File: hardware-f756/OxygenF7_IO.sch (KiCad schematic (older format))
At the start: 13 parts, among them J10 Micro_SD_Card_Det, J3 JST SH-4, J4 JST ZH-4, J5 Conn_03x08, J6 Conn_01x16, J7 Conn_01x04, J9 JST GH-6, U3 MPU-6000, U4 BMP388

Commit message: Swap out some out-of-stock parts
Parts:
- C19, C20, C22: Part# CL21B104KACNNNC -> CL21B104KBCNNNC‎
- C21: Part# CL21B104KACNNNC -> CL21B222KBANNNC
- J3: footprint Connector_JST:JST_SH_BM04B-SRSS-TB_1x04-1MP_P1.00mm_Vertical -> Connector_JST:JST_SH_SM04B-SRSS-TB_1x04-1MP_P1.00mm_Horizontal; Part# BM04B-SRSS-TB(LF)(SN) -> SM04B-SRSS-TB(LF)(SN)
- J9: value JST GH-6 -> 1.25mm; footprint Connector_JST:JST_GH_BM06B-GHS-TBT_1x06-1MP_P1.25mm_Vertical -> Sonrise:10114830-10106LF_P1.25mm_Horizontal; Part# BM04B-GHS-TBT(LF)(SN)(N) -> 10114830-10106LF
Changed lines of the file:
@@
 F 0 "J3" H 4068 775 50  0000 C CNN
 F 1 "JST SH-4" H 4068 866 50  0000 C CNN
-F 2 "Connector_JST:JST_SH_BM04B-SRSS-TB_1x04-1MP_P1.00mm_Vertical" H 4150 1200 50  0001 C CNN
+F 2 "Connector_JST:JST_SH_SM04B-SRSS-TB_1x04-1MP_P1.00mm_Horizontal" H 4150 1200 50  0001 C CNN
 F 3 "~" H 4150 1200 50  0001 C CNN
-F 4 "BM04B-SRSS-TB(LF)(SN)" H 4150 1200 50  0001 C CNN "Part#"
+F 4 "SM04B-SRSS-TB(LF)(SN)" H 4150 1200 50  0001 C CNN "Part#"
 	1    4150 1200
 	-1   0    0    1
@@
 F 2 "Capacitor_SMD:C_0805_2012Metric" H 2488 3450 50  0001 C CNN
 F 3 "~" H 2450 3600 50  0001 C CNN
-F 4 "CL21B104KACNNNC" H 2450 3600 50  0001 C CNN "Part#"
+F 4 "CL21B104KBCNNNC‎" H 2450 3600 50  0001 C CNN "Part#"
 	1    2450 3600
 	1    0    0    -1
@@
 F 2 "Capacitor_SMD:C_0805_2012Metric" H 3088 2000 50  0001 C CNN
 F 3 "~" H 3050 2150 50  0001 C CNN
-F 4 "CL21B104KACNNNC" H 3050 2150 50  0001 C CNN "Part#"
+F 4 "CL21B222KBANNNC" H 3050 2150 50  0001 C CNN "Part#"
 	1    3050 2150
 	1    0    0    -1
@@
 F 2 "Capacitor_SMD:C_0805_2012Metric" H 2688 2000 50  0001 C CNN
 F 3 "~" H 2650 2150 50  0001 C CNN
-F 4 "CL21B104KACNNNC" H 2650 2150 50  0001 C CNN "Part#"
+F 4 "CL21B104KBCNNNC‎" H 2650 2150 50  0001 C CNN "Part#"
 	1    2650 2150
 	1    0    0    -1
@@
 F 2 "Capacitor_SMD:C_0805_2012Metric" H 3538 1500 50  0001 C CNN
 F 3 "~" H 3500 1650 50  0001 C CNN
-F 4 "CL21B104KACNNNC" H 3500 1650 50  0001 C CNN "Part#"
+F 4 "CL21B104KBCNNNC‎" H 3500 1650 50  0001 C CNN "Part#"
 	1    3500 1650
 	1    0    0    -1
@@
 AR Path="/60FE74E7/61026A51" Ref="J9"  Part="1"
 F 0 "J9" H 4068 3075 50  0000 C CNN
-F 1 "JST GH-6" H 4068 3166 50  0000 C CNN
-F 2 "Connector_JST:JST_GH_BM06B-GHS-TBT_1x06-1MP_P1.25mm_Vertical" H 4150 3600 50  0001 C CNN
+F 1 "1.25mm" H 4068 3166 50  0000 C CNN
+F 2 "Sonrise:10114830-10106LF_P1.25mm_Horizontal" H 4150 3600 50  0001 C CNN
 F 3 "~" H 4150 3600 50  0001 C CNN
-F 4 "BM04B-GHS-TBT(LF)(SN)(N)" H 4150 3600 50  0001 C CNN "Part#"
+F 4 "10114830-10106LF" H 4150 3600 50  0001 C CNN "Part#"
 	1    4150 3600
 	-1   0    0    1

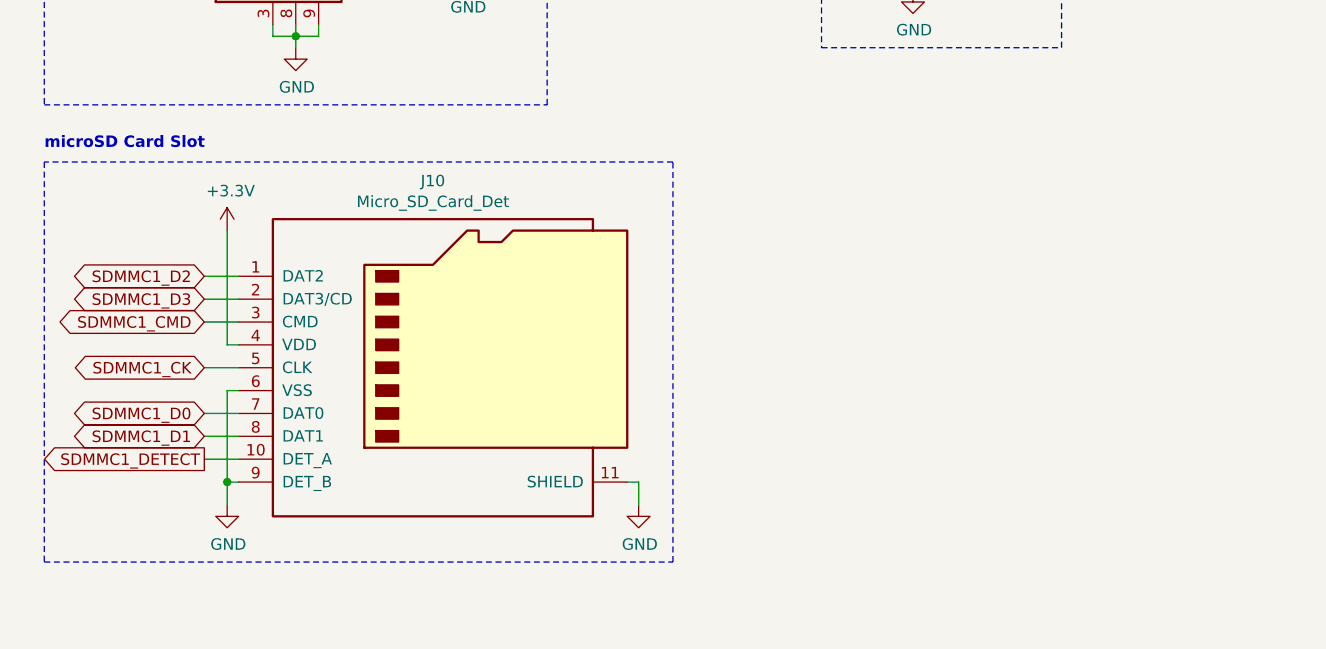
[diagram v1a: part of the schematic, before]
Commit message: Don't ground unused MCU pins and add microSD pull-up resistors
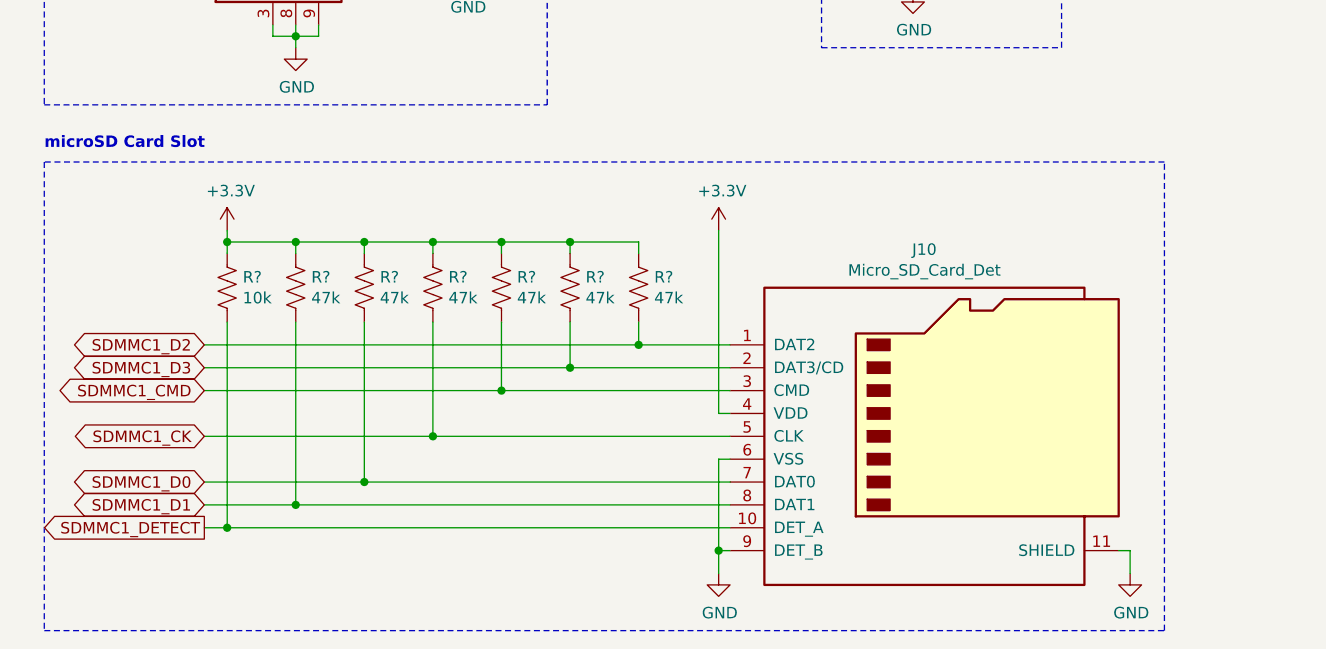
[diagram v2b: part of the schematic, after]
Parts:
- added R?: 10k, symbol Device:R_US
- added R? (x6): 47k, symbol Device:R_US
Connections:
- net +3V3: now also R?.1, R?.1, R?.1, R?.1, R?.1, R?.1, R?.1
- net SDMMC1_CK: now also R?.2
- net SDMMC1_CMD: now also R?.2
- net SDMMC1_D0: now also R?.2
- net SDMMC1_D1: now also R?.2
- net SDMMC1_D2: now also R?.2
- net SDMMC1_D3: now also R?.2
- net SDMMC1_DETECT: now also R?.2
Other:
- moved on the sheet: J10

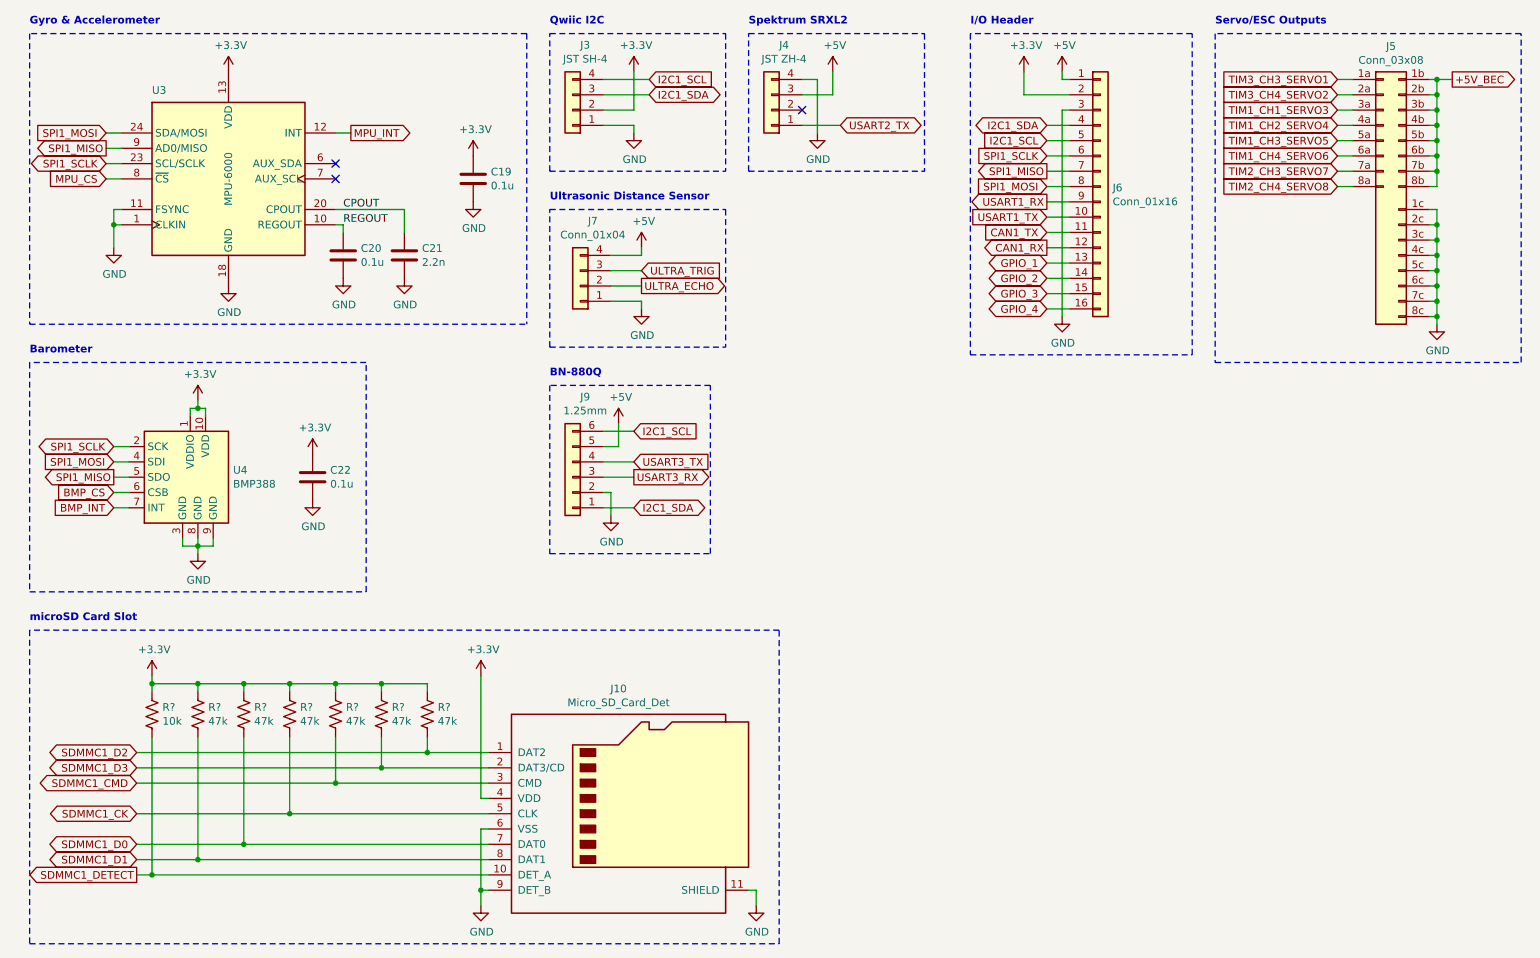
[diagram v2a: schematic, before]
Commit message: Add more pull-up/pull-down resistors and 128MB flash memory
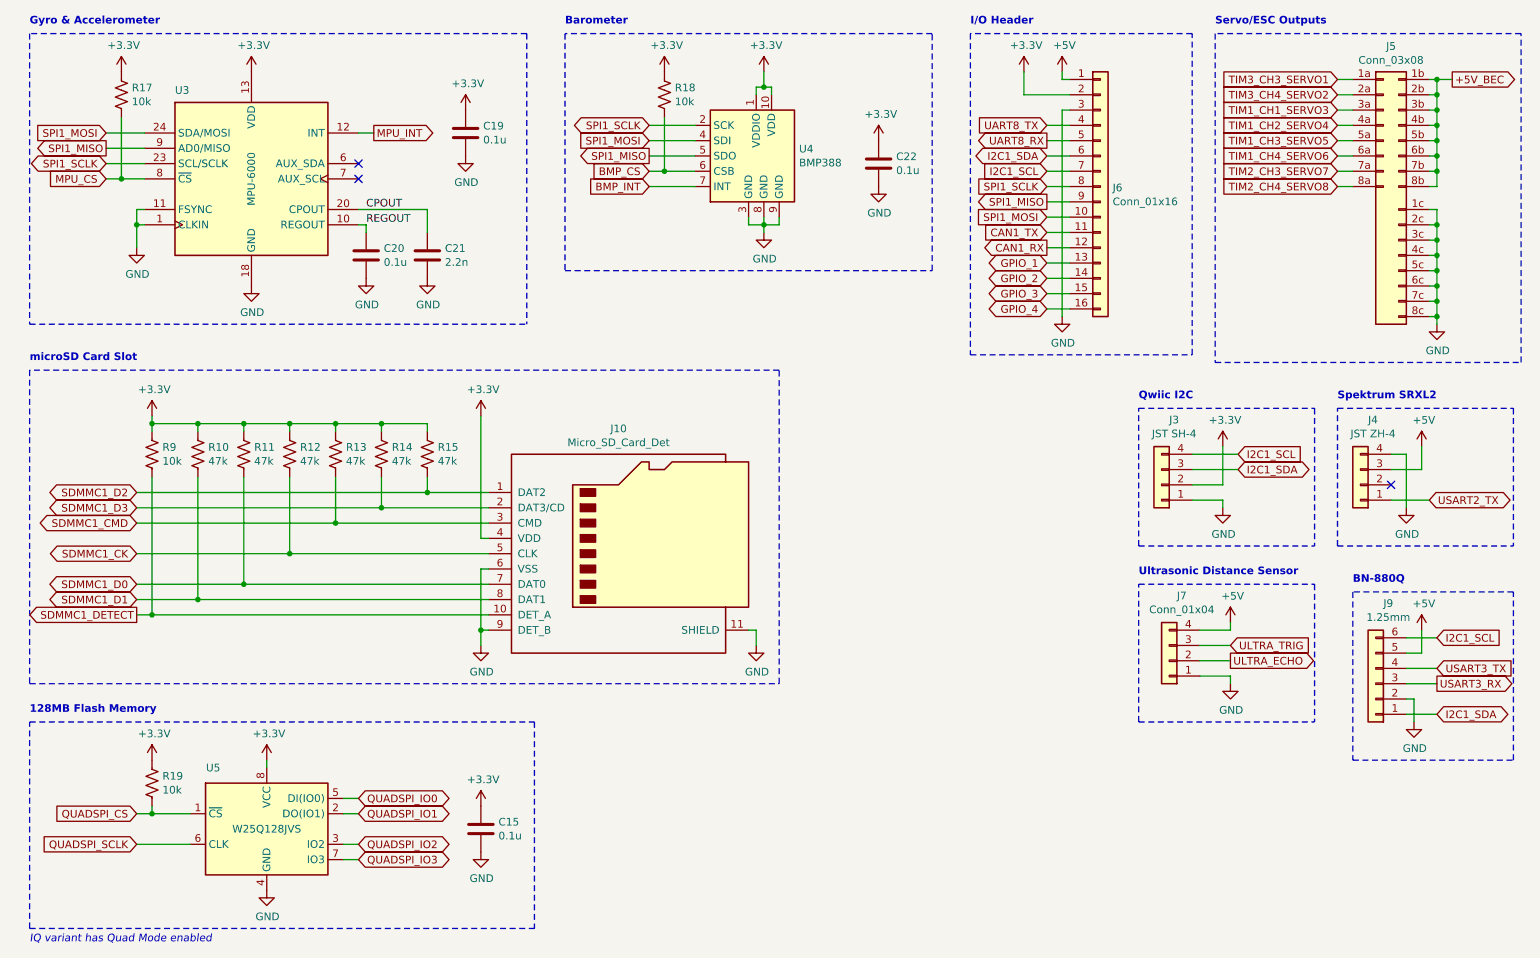
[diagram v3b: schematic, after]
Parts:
- added C15: 0.1u, Capacitor_SMD:C_0805_2012Metric, symbol Device:C
- added R17, R18, R19: 10k, Resistor_SMD:R_0805_2012Metric, symbol Device:R_US
- added U5: W25Q128JVS, Package_SO:SOIC-8_5.23x5.23mm_P1.27mm, symbol Memory_Flash:W25Q128JVS
- R10, R11, R12, R13, R14, R15: renamed from R?; footprint (none) -> Resistor_SMD:R_0805_2012Metric; Part# (none) -> RMCF0805JT47K0
- R9: renamed from R?; footprint (none) -> Resistor_SMD:R_0805_2012Metric; Part# (none) -> RMCF0805FT10K0
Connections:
- net USART1_RX is gone; now on net SPI1_MISO: J6.9 (Pin_9)
- net USART1_TX is gone; now on net SPI1_MOSI: J6.10 (Pin_10)
- net +3V3: now also C15.1, R17.1, R18.1, R19.1, U5.8 (VCC)
- net BMP_CS: now also R18.2
- net GND: now also C15.2, U5.4 (GND)
- net I2C1_SCL: now also J6.7 (Pin_7); no longer J6.5 (Pin_5)
- net I2C1_SDA: now also J6.6 (Pin_6); no longer J6.4 (Pin_4)
- net MPU_CS: now also R17.2
- net SPI1_MISO: no longer J6.7 (Pin_7)
- net SPI1_MOSI: no longer J6.8 (Pin_8)
- net SPI1_SCLK: now also J6.8 (Pin_8); no longer J6.6 (Pin_6)
- new net QUADSPI_CS: R19.2, U5.1 (~CS)
- new net QUADSPI_IO0: U5.5 (DI(IO0))
- new net QUADSPI_IO1: U5.2 (DO(IO1))
- new net QUADSPI_IO2: U5.3 (IO2)
- new net QUADSPI_IO3: U5.7 (IO3)
- new net QUADSPI_SCLK: U5.6 (CLK)
- new net UART8_RX: J6.5 (Pin_5)
- new net UART8_TX: J6.4 (Pin_4)
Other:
- note added: "128MB Flash Memory"
- note added: "IQ variant has Quad Mode enabled"
- moved on the sheet: C19, C20, C21, C22, J10, J3, J4, J7, J9, R10, R11, R12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

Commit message: New board layout
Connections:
- net CAN1_RX: now also J6.16 (Pin_16); no longer J6.12 (Pin_12)
- net CAN1_TX: now also J6.15 (Pin_15); no longer J6.11 (Pin_11)
- net GPIO_1: now also J6.11 (Pin_11); no longer J6.13 (Pin_13)
- net GPIO_2: now also J6.12 (Pin_12); no longer J6.14 (Pin_14)
- net GPIO_3: now also J6.13 (Pin_13); no longer J6.15 (Pin_15)
- net GPIO_4: now also J6.14 (Pin_14); no longer J6.16 (Pin_16)
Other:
- moved on the sheet: J3, J4, J7, J9
